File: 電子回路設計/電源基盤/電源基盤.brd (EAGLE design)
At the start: 165 x 36 mm, 59 parts, among them IC1 FDS4935A, IC2 NJM7805FA-I, SW1 SS-12D01-VG4, T1 TLP291, T2 TLP291, T3 TJ60S04M3L, T4 TLP291, T5 IRLML6344TRPBF

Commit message: point : circuit desgine comp
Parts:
- removed JP4: (no value), pinhead:1X08
- added JP1, JP2: (no value), pinhead:2X08
- JP3: device pinhead:1X08 -> pinhead:1X09
- moved JP3 88.4 mm to (172.0, 0.00), turned to 270 degrees
- moved HOME 22.0 mm to (161.0, -11.0)
- moved 5V 18.0 mm to (8.00, -6.50)
- moved A_FAN 18.0 mm to (17.5, -14.5)
- moved BP 18.0 mm to (8.00, -9.00)
- moved BPS 18.0 mm to (8.00, -4.00)
- moved BZ1 18.0 mm to (19.8, -4.00)
- moved C1 18.0 mm to (43.0, 13.0)
- moved C13 18.0 mm to (70.8, -2.10)
- moved C14 18.0 mm to (70.8, 2.00)
- moved C15 18.0 mm to (36.2, -2.50)
- moved C17 18.0 mm to (67.5, -5.00)
- moved C2 18.0 mm to (43.0, -13.0)
- moved C3 18.0 mm to (113.5, -6.50)
- moved C4 18.0 mm to (95.0, 0.00)
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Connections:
- new net A_IS1: JP1.10, JP3.5
- new net A_IS2: JP1.12, JP3.6
- new net EN: JP1.6, JP3.3
- new net LPWM: JP1.8, JP3.4
- new net LS1: JP1.14, JP3.7
- new net LS2: JP1.16, JP3.8
- new net RPWM: JP1.4, JP3.2
- net +5V: now also JP1.1, JP1.2, JP2.1, JP2.2; no longer JP4.1
- net BUZ: now also JP2.4; no longer JP4.2
- net ERR_LED: now also JP2.6; no longer JP4.3
- net GND: now also JP1.11, JP1.13, JP1.15, JP1.3, JP1.5, JP1.7, JP1.9, JP2.11, JP2.12, JP2.13, JP2.15, JP2.16, JP2.3, JP2.5, JP2.7, JP2.9, JP3.9; no longer JP3.8, JP4.8
- net HOME_SW: now also JP2.14; no longer JP4.7
- net PR_LED: now also JP2.8; no longer JP4.4
- net PW_AD: now also JP2.10; no longer JP4.5
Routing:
- net RPWM: track 0.00 -> 107.6 mm
- net EN: track 0.00 -> 102.9 mm
- net +5V: track 170.0 -> 271.7 mm
- net LPWM: track 0.00 -> 98.1 mm
- net A_IS1: track 0.00 -> 92.7 mm
- net A_IS2: track 0.00 -> 89.1 mm
- net LS1: track 0.00 -> 86.8 mm
- net LS2: track 0.00 -> 86.1 mm
- net PW_AD: track 107.1 -> 130.9 mm, vias 0 -> 1
- net ERR_LED: track 82.6 -> 80.2 mm, vias 1 -> 0
- net PR_LED: track 84.8 -> 82.6 mm, vias 1 -> 0
- net BUZ: track 57.8 -> 56.2 mm, vias 1 -> 0
- net N$8: track 40.7 -> 39.6 mm
- net HOME_SW: track 73.3 -> 72.5 mm
- net VDD: track 111.3 -> 110.7 mm
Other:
- board size 165 x 36 mm -> 175 x 36 mm
- board text added: "5V"
- board text added: "A_IS1"
- board text added: "A_IS2"
- board text added: "EN"
- board text added: "GND"
- board text added: "LPWM"
- board text added: "LS1"
- board text added: "LS2"
- board text added: "RPWM"

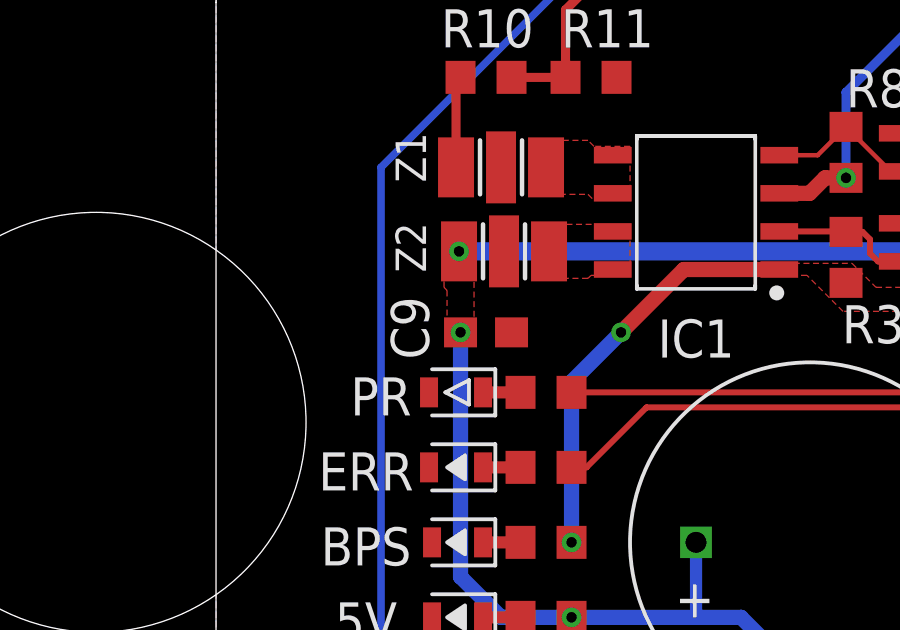
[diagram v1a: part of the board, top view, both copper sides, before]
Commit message: fix : cam data
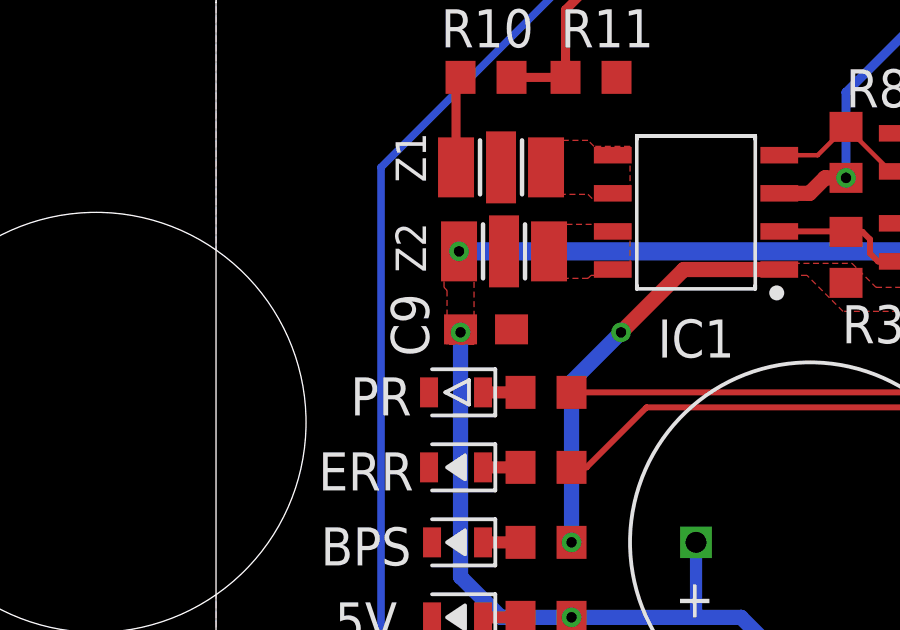
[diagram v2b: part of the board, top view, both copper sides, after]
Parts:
- moved C9 0.10 mm to (9.00, 3.10)
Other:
- board text added: "A_FAN"
- board text added: "BP"
- board text added: "BPS"
- board text added: "BZ1"
- board text added: "C1"
- board text added: "C13"
- board text added: "C14"
- board text added: "C15"
- board text added: "C17"
- board text added: "C2"
- board text added: "C3"
- board text added: "C4"
- board text added: "C5"
- board text added: "C9"
- board text added: "CN1"
- board text added: "CN2"
- board text added: "CN3"
- board text added: "CN4"
- board text added: "D1"
- board text added: "D2"
- board text added: "D3"
- board text added: "ERR"
- board text added: "HOME"
- board text added: "IC1"
- board text added: "IC2"
- board text added: "JP1"
- board text added: "JP2"
- board text added: "JP3"
- board text added: "L_AM_P"
- board text added: "PL"
- board text added: "PR"
- board text added: "R1"
- board text added: "R10"
- board text added: "R11"
- board text added: "R12"
- board text added: "R13"
- board text added: "R14"
- board text added: "R15"
- board text added: "R2"
- board text added: "R3"
- board text added: "R39"
- board text added: "R4"
- board text added: "R42"
- board text added: "R5"
- board text added: "R6"
- board text added: "R7"
- board text added: "R8"
- board text added: "R9"
- board text added: "R_AM_P"
- board text added: "SW1"
- board text added: "T1"
- board text added: "T2"
- board text added: "T3"
- board text added: "T4"
- board text added: "T5"
- board text added: "UM_P+"
- board text added: "UM_P-"
- board text added: "Z1"
- board text added: "Z2"
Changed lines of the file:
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@@
 <setting verticaltext="up"/>
 </settings>
-<grid distance="1" unitdist="mm" unit="mm" style="lines" multiple="1" display="yes" altdistance="5" altunitdist="mil" altunit="mil"/>
+<grid distance="10" unitdist="mm" unit="mm" style="lines" multiple="1" display="yes" altdistance="5" altunitdist="mil" altunit="mil"/>
 <layers>
 <layer number="1" name="Top" color="4" fill="1" visible="yes" active="yes"/>
@@
 <layer number="113" name="IDFDebug" color="7" fill="1" visible="yes" active="yes"/>
 <layer number="116" name="Patch_BOT" color="7" fill="1" visible="yes" active="yes"/>
-<layer number="121" name="_tsilk" color="7" fill="1" visible="yes" active="yes"/>
-<layer number="122" name="_bsilk" color="7" fill="1" visible="yes" active="yes"/>
+<layer number="121" name="_tPlace" color="14" fill="1" visible="yes" active="yes"/>
+<layer number="122" name="_bPlace" color="5" fill="1" visible="yes" active="yes"/>
 <layer number="123" name="tTestmark" color="7" fill="1" visible="yes" active="yes"/>
 <layer number="124" name="bTestmark" color="7" fill="1" visible="yes" active="yes"/>
-<layer number="125" name="_tNames" color="7" fill="1" visible="yes" active="yes"/>
-<layer number="126" name="_bNames" color="7" fill="1" visible="yes" active="yes"/>
+<layer number="125" name="_tNames" color="14" fill="1" visible="yes" active="yes"/>
+<layer number="126" name="_bNames" color="5" fill="1" visible="yes" active="yes"/>
 <layer number="127" name="_tValues" color="7" fill="1" visible="yes" active="yes"/>
 <layer number="128" name="_bValues" color="7" fill="1" visible="yes" active="yes"/>
@@
 <circle x="77" y="-16" radius="2" width="0.2" layer="21"/>
 <hole x="148.5" y="0" drill="3.2"/>
+<text x="4.999990625" y="-5.9999875" size="1.27" layer="125" rot="R180" align="bottom-center">5V</text>
+<text x="23.500003125" y="-16.699990625" size="1.27" layer="125" ratio="10" rot="R90">A_FAN</text>
+<text x="4.999990625" y="-8.500009375" size="1.27" layer="125" rot="R180" align="bottom-center">BP</text>
+<text x="4.999990625" y="-3.49999375" size="1.27" layer="125" rot="R180" align="bottom-center">BPS</text>
+<text x="13.599996875" y="-7.700009375" size="1.016" layer="125" rot="R270">BZ1</text>
+<text x="45.500009375" y="12.5" size="1.27" layer="125" rot="R90">C1</text>
+<text x="43.634990625" y="-12.365" size="1.27" layer="125" rot="R270">C2</text>
+<text x="114.135003125" y="-5.8650125" size="1.27" layer="125" rot="R270">C3</text>
+<text x="85.00000625" y="-4.499990625" size="1.778" layer="125" rot="R90">C4</text>
+<text x="4.999990625" y="-13" size="1.016" layer="121" rot="R270">C5</text>
+<text x="7.1000125" y="2.199996875" size="1.27" layer="125" rot="R90">C9</text>
+<text x="71.249996875" y="-7.1000125" size="1.27" layer="125" rot="R90">C13</text>
+<text x="71.249996875" y="4.250003125" size="1.27" layer="125" rot="R90">C14</text>
+<text x="40.134996875" y="-6.5000125" size="1.27" layer="125" rot="R270" align="bottom-center">C15</text>
+<text x="68.134990625" y="-5.634990625" size="1.27" layer="125" rot="R180">C17</text>
+<text x="143.799990625" y="-10.500003125" size="1.27" layer="125" ratio="10">CN1</text>
+<text x="156.19999375" y="11.500003125" size="1.27" layer="125" ratio="10" rot="R180">CN2</text>
+<text x="127.999996875" y="-14.499996875" size="1.27" layer="125" ratio="10" rot="R180">CN3</text>
+<text x="127.999996875" y="4.499990625" size="1.27" layer="125" ratio="10" rot="R180">CN4</text>
+<text x="41.48490625" y="2.49999375" size="1.27" layer="125" rot="R270" align="bottom-center">D1</text>
+<text x="11.000003125" y="15.99999375" size="1.27" layer="125" rot="R180" align="bottom-center">D2</text>
+<text x="43.9849" y="2.49999375" size="1.27" layer="125" rot="R270" align="bottom-center">D3</text>
+<text x="4.999990625" y="-0.999996875" size="1.27" layer="125" rot="R180" align="bottom-center">ERR</text>
+<text x="164.000003125" y="-5.9999875" size="1.27" layer="122" rot="MR0">HOME</text>
+<text x="15.99999375" y="3.43009375" size="1.27" layer="125" rot="R180" align="bottom-center">IC1</text>
+<text x="55.79300625" y="-3.81" size="1.778" layer="125" ratio="10" rot="R90">IC2</text>
+<text x="79.839996875" y="16.175" size="1.27" layer="125" ratio="10">JP1</text>
+<text x="79.839996875" y="-9.825" size="1.27" layer="125" ratio="10">JP2</text>
+<text x="169.999990625" y="12" size="1.27" layer="125" ratio="10">JP3</text>
+<text x="31.4999875" y="10.00000625" size="1.27" layer="125" ratio="10" rot="R90">L_AM_P</text>
+<text x="163.40490625" y="0" size="1.27" layer="126" rot="MR90" align="bottom-center">PL</text>
+<text x="5.4999875" y="1.499996875" size="1.27" layer="125" rot="R180" align="bottom-center">PR</text>
+<text x="37.1149875" y="2.61500625" size="1.27" layer="125" rot="R90">R1</text>
+<text x="13" y="-9.50000625" size="1.27" layer="126" rot="MR0">R2</text>
+<text x="13" y="-7.0000125" size="1.27" layer="126" rot="MR0">R3</text>
+<text x="156.63499375" y="3.364990625" size="1.27" layer="125" rot="R180">R4</text>
+<text x="32.5000125" y="7.2000125" size="1.27" layer="125" rot="R270">R5</text>
+<text x="147.500009375" y="8.500009375" size="1.27" layer="125">R6</text>
+<text x="159.1349875" y="0.635" size="1.27" layer="126" rot="MR0">R7</text>
+<text x="21.000009375" y="10.500003125" size="1.27" layer="125">R8</text>
+<text x="27.499996875" y="12.5" size="1.27" layer="125">R9</text>
+<text x="7.500009375" y="12.5" size="1.27" layer="125">R10</text>
+<text x="11.500003125" y="12.5" size="1.27" layer="125">R11</text>
+<text x="13" y="0.5" size="1.27" layer="126" rot="MR0">R12</text>
+<text x="13" y="-1.999996875" size="1.27" layer="126" rot="MR0">R13</text>
+<text x="29.73499375" y="-8.035009375" size="1.27" layer="125" rot="R180">R14</text>
+<text x="28.46499375" y="-8.86500625" size="1.27" layer="125">R15</text>
+<text x="20.86500625" y="2.634996875" size="1.27" layer="125">R39</text>
+<text x="13" y="-4.499990625" size="1.27" layer="126" rot="MR0">R42</text>
+<text x="40.49999375" y="-10.00000625" size="1.27" layer="125" ratio="10" rot="R270">R_AM_P</text>
+<text x="157.9999875" y="2.99999375" size="1.27" layer="126" rot="MR90">SW1</text>
+<text x="26" y="5.4999875" size="1.27" layer="125" align="bottom-center">T1</text>
+<text x="153.999996875" y="8.500009375" size="1.27" layer="125" align="bottom-center">T2</text>
+<text x="139.5" y="2.49999375" size="1.016" layer="125" rot="R270">T3</text>
+<text x="26" y="8.29990625" size="1.27" layer="125" align="bottom-center">T4</text>
+<text x="25.9" y="-11.4435875" size="1.27" layer="125" rot="R180" align="bottom-center">T5</text>
+<text x="111.00000625" y="-14.499996875" size="1.27" layer="125" ratio="10" rot="R180">UM_P+</text>
+<text x="111.00000625" y="4.499990625" size="1.27" layer="125" ratio="10" rot="R180">UM_P-</text>
+<text x="7.0000125" y="8.000009375" size="1.016" layer="125" ratio="18" rot="R90">Z1</text>
+<text x="7.0000125" y="4.999990625" size="1.016" layer="125" ratio="18" rot="R90">Z2</text>
 </plain>
 <attributes>
@@
 <attribute name="VALUE" x="38.5151" y="2.5" size="1.27" layer="27" rot="R270" align="top-center"/>
 </element>
-<element name="C9" library="rcl" package="C0603" package3d_urn="urn:adsk.eagle:package:23616/2" value="0.1u" x="9" y="3" smashed="yes">
-<attribute name="NAME" x="7.1" y="2.1" size="1.27" layer="25" rot="R90"/>
-<attribute name="POPULARITY" value="73" x="-279" y="31" size="1.778" layer="27" display="off"/>
-<attribute name="SPICEPREFIX" value="C" x="-279" y="31" size="1.778" layer="27" display="off"/>
-<attribute name="VALUE" x="8.365" y="1.095" size="1.27" layer="27"/>
+<element name="C9" library="rcl" package="C0603" package3d_urn="urn:adsk.eagle:package:23616/2" value="0.1u" x="9" y="3.1" smashed="yes">
+<attribute name="NAME" x="7.1" y="2.2" size="1.27" layer="25" rot="R90"/>
+<attribute name="POPULARITY" value="73" x="-279" y="31.1" size="1.778" layer="27" display="off"/>
+<attribute name="SPICEPREFIX" value="C" x="-279" y="31.1" size="1.778" layer="27" display="off"/>
+<attribute name="VALUE" x="8.365" y="1.195" size="1.27" layer="27"/>
 </element>
 <element name="Z2" library="EMIフィルタ" package="NFE31" package3d_urn="urn:adsk.eagle:package:29147495/2" value="NFE31PT" x="9.6" y="5.7" smashed="yes" rot="R180">
